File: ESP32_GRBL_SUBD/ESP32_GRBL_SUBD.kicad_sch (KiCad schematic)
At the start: 65 parts, among them J1 DB25_Female_MountingHoles, J10 Screw_Terminal_01x02, J11 Screw_Terminal_01x02, J12 Screw_Terminal_01x02, J13 Screw_Terminal_01x02, J14 Screw_Terminal_01x02, J2 Micro_SD_Card, J3 Conn_01x19_Female, J3a1 Conn_01x19_Female, J4 Conn_01x19_Female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

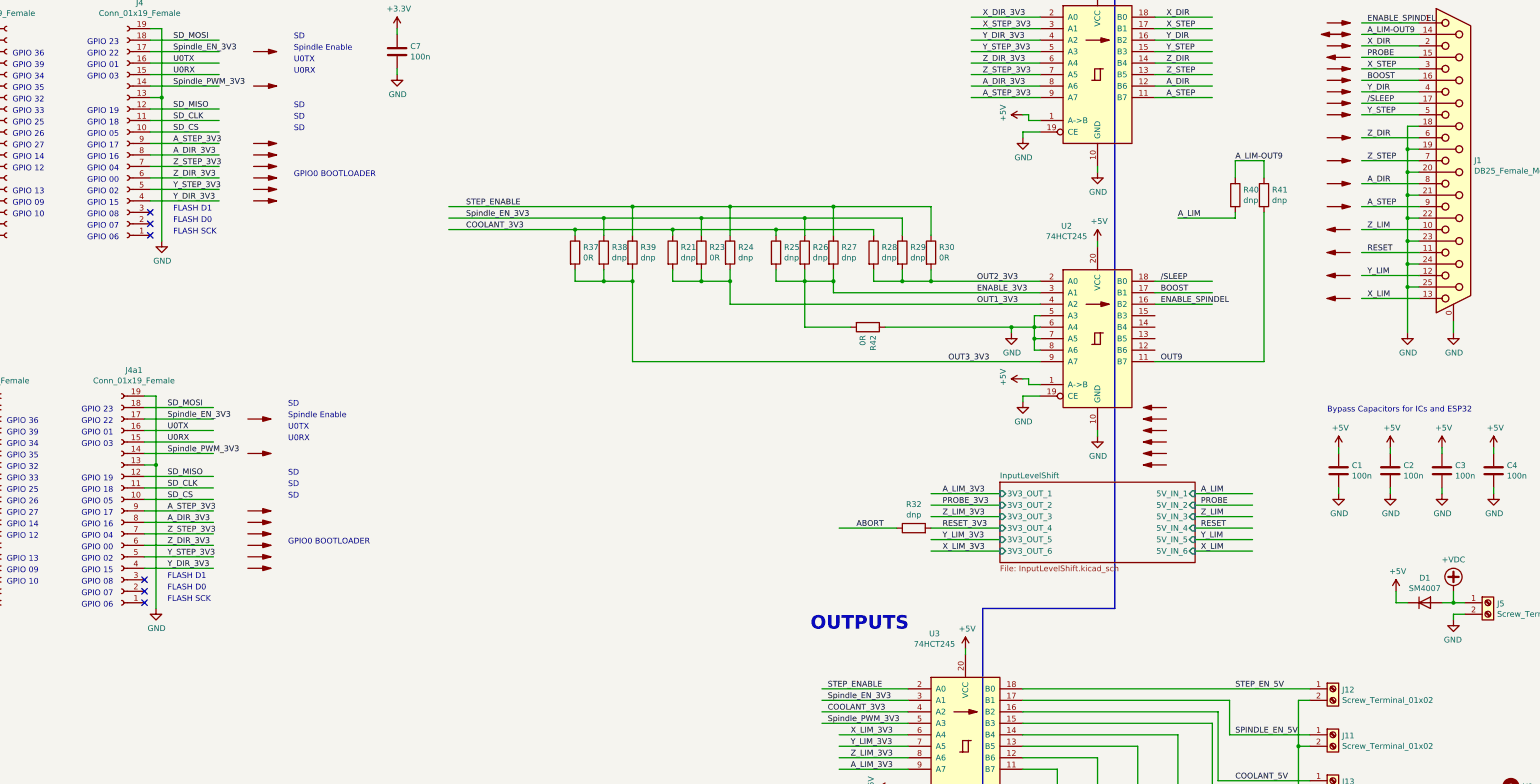
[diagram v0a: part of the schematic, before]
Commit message: wired Axis a to screw terminals
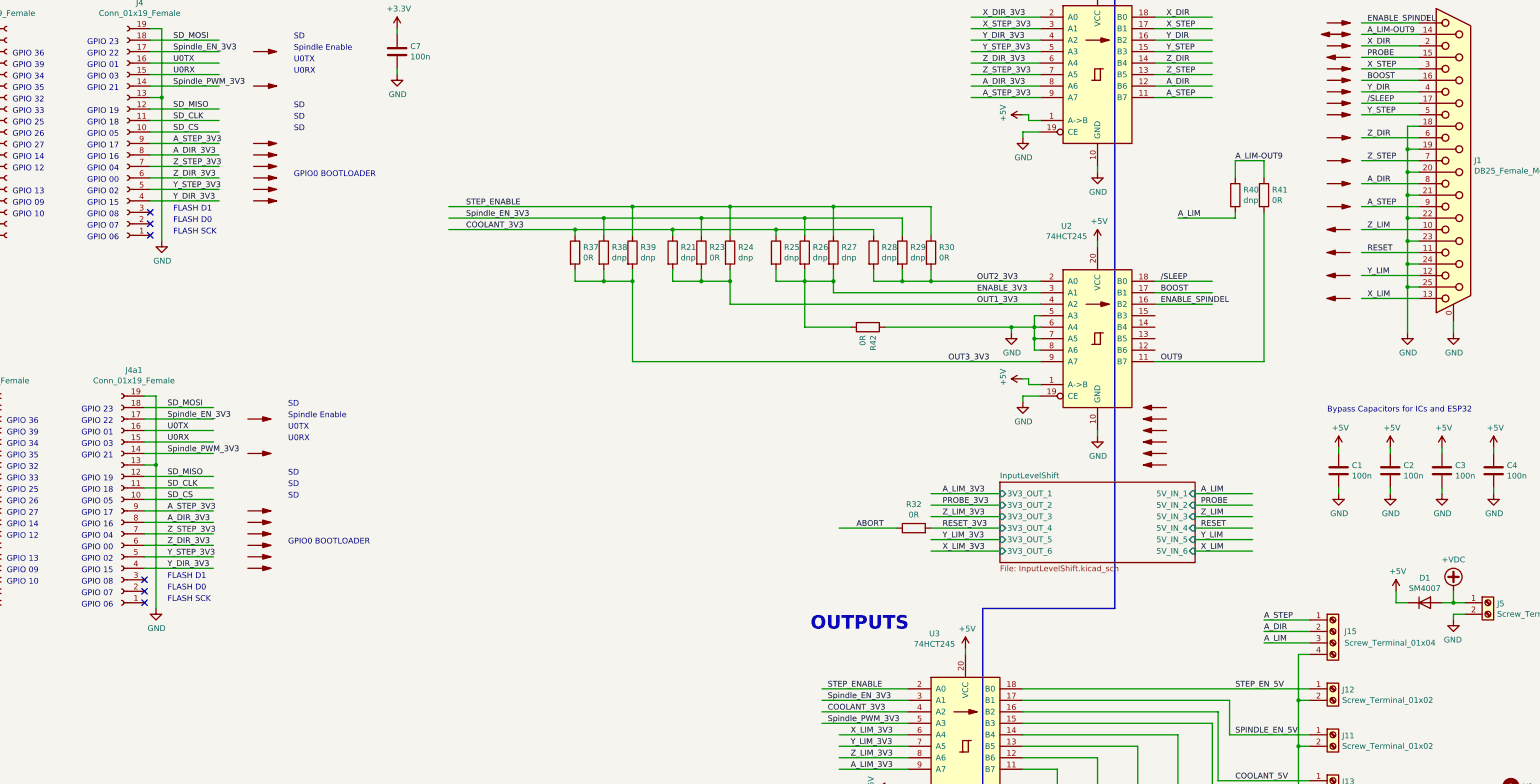
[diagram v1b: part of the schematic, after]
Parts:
- added J15: Screw_Terminal_01x04, TerminalBlock_MetzConnect:TerminalBlock_MetzConnect_Type055_RT01504HDWU_1x04_P5.00mm_Horizontal, symbol Connector:Screw_Terminal_01x04
- R32, R41: value dnp -> 0R
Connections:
- net A_DIR: now also J15.2 (Pin_2)
- net A_LIM: now also J15.3 (Pin_3)
- net A_STEP: now also J15.1 (Pin_1)
- net GND: now also J15.4 (Pin_4)
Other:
- note added: "GPIO 21"
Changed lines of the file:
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@@
   (junction (at 274.32 99.06) (diameter 0) (color 0 0 0 0)
   )
+  (junction (at 337.82 181.61) (diameter 0) (color 0 0 0 0)
+  )
   (junction (at 256.54 88.9) (diameter 0) (color 0 0 0 0)
   )
@@
     (stroke (width 0) (type default) (color 0 0 0 0))
   )
+  (wire (pts (xy 330.2 163.83) (xy 340.36 163.83))
+    (stroke (width 0) (type default) (color 0 0 0 0))
+  )
   (wire (pts (xy 149.86 72.39) (xy 190.5 72.39))
     (stroke (width 0) (type default) (color 0 0 0 0))
@@
     (stroke (width 0) (type default) (color 0 0 0 0))
   )
+  (wire (pts (xy 340.36 171.45) (xy 337.82 171.45))
+    (stroke (width 0) (type default) (color 0 0 0 0))
+  )
   (wire (pts (xy 67.31 247.65) (xy 90.17 247.65))
     (stroke (width 0) (type default) (color 0 0 0 0))
@@
     (stroke (width 0) (type default) (color 0 0 0 0))
   )
+  (wire (pts (xy 330.2 168.91) (xy 340.36 168.91))
+    (stroke (width 0) (type default) (color 0 0 0 0))
+  )
   (wire (pts (xy 31.75 60.96) (xy 46.99 60.96))
     (stroke (width 0) (type default) (color 0 0 0 0))
@@
     (stroke (width 0) (type default) (color 0 0 0 0))
   )
+  (wire (pts (xy 330.2 166.37) (xy 340.36 166.37))
+    (stroke (width 0) (type default) (color 0 0 0 0))
+  )
   (wire (pts (xy 276.86 189.23) (xy 311.15 189.23))
     (stroke (width 0) (type default) (color 0 0 0 0))
@@
     (stroke (width 0) (type default) (color 0 0 0 0))
   )
+  (wire (pts (xy 337.82 171.45) (xy 337.82 181.61))
+    (stroke (width 0) (type default) (color 0 0 0 0))
+  )
   (wire (pts (xy 264.16 212.09) (xy 264.16 214.63))
     (stroke (width 0) (type default) (color 0 0 0 0))
@@
     (effects (font (size 1.27 1.27)) (justify left bottom))
   )
+  (text "GPIO 21" (at 68.58 128.27 0)
+    (effects (font (size 1.27 1.27)) (justify left bottom))
+  )
   (text "SD" (at 114.3 116.84 0)
     (effects (font (size 1.27 1.27)) (justify left bottom))
@@
     (effects (font (size 1.27 1.27)) (justify left bottom))
   )
+  (text "GPIO 21" (at 69.85 46.99 0)
+    (effects (font (size 1.27 1.27)) (justify left bottom))
+  )
   (text "GPIO 09" (at 52.07 153.67 0)
     (effects (font (size 1.27 1.27)) (justify left bottom))
@@
     (effects (font (size 1.27 1.27)) (justify left bottom))
   )
+  (label "A_DIR" (at 330.2 166.37 0)
+    (effects (font (size 1.27 1.27)) (justify left bottom))
+  )
   (label "A_STEP_3V3" (at 88.9 58.42 0)
     (effects (font (size 1.27 1.27)) (justify left bottom))
@@
     (effects (font (size 1.27 1.27)) (justify left bottom))
   )
+  (label "A_LIM" (at 330.2 168.91 0)
+    (effects (font (size 1.27 1.27)) (justify left bottom))
+  )
   (label "BOOST" (at 353.06 44.45 0)
     (effects (font (size 1.27 1.27)) (justify left bottom))
@@
     (effects (font (size 1.27 1.27)) (justify left bottom))
   )
+  (label "A_STEP" (at 330.2 163.83 0)
+    (effects (font (size 1.27 1.27)) (justify left bottom))
+  )
   (label "Z_STEP_3V3" (at 88.9 63.5 0)
     (effects (font (size 1.27 1.27)) (justify left bottom))
@@
     (in_bom yes) (on_board yes)
     (property "Reference" "R32" (id 0) (at 252.73 138.2522 90))
-    (property "Value" "dnp" (id 1) (at 252.73 140.5636 90))
+    (property "Value" "0R" (id 1) (at 252.73 140.5636 90))
     (property "Footprint" "Resistor_SMD:R_0603_1608Metric" (id 2) (at 252.73 145.288 90)
       (effects (font (size 1.27 1.27)) hide)
@@
       (effects (font (size 1.27 1.27)) (justify left))
     )
-    (property "Value" "dnp" (id 1) (at 331.978 70.993 0)
+    (property "Value" "0R" (id 1) (at 331.978 70.993 0)
       (effects (font (size 1.27 1.27)) (justify left))
     )
@@
     )
   )
+  (symbol (lib_id "Connector:Screw_Terminal_01x04") (at 345.44 166.37 0) (unit 1)
+    (in_bom yes) (on_board yes) (fields_autoplaced)
+    (property "Reference" "J15" (id 0) (at 347.98 166.3699 0)
+      (effects (font (size 1.27 1.27)) (justify left))
+    )
+    (property "Value" "Screw_Terminal_01x04" (id 1) (at 347.98 168.9099 0)
+      (effects (font (size 1.27 1.27)) (justify left))
+    )
+    (property "Footprint" "TerminalBlock_MetzConnect:TerminalBlock_MetzConnect_Type055_RT01504HDWU_1x04_P5.00mm_Horizontal" (id 2) (at 345.44 166.37 0)
+      (effects (font (size 1.27 1.27)) hide)
+    )
+    (property "Datasheet" "~" (id 3) (at 345.44 166.37 0)
+      (effects (font (size 1.27 1.27)) hide)
+    )
+    (pin "1")
+    (pin "2")
+    (pin "3")
+    (pin "4")
+  )
   (symbol (lib_id "Connector:Screw_Terminal_01x02") (at 238.76 228.6 0) (unit 1)
     (in_bom yes) (on_board yes)
@@
       (reference "J14") (unit 1) (value "Screw_Terminal_01x02") (footprint "TerminalBlock_MetzConnect:TerminalBlock_MetzConnect_Type055_RT01502HDWU_1x02_P5.00mm_Horizontal")
     )
+    (path "/cfbb8e34-21a6-469a-90d0-36c5e2e8a754"
+      (reference "J15") (unit 1) (value "Screw_Terminal_01x04") (footprint "TerminalBlock_MetzConnect:TerminalBlock_MetzConnect_Type055_RT01504HDWU_1x04_P5.00mm_Horizontal")
+    )
     (path "/00000000-0000-0000-0000-00005f4ee6a6/00000000-0000-0000-0000-00005f4f5669"
       (reference "Q2") (unit 1) (value "BSS138") (footprint "Package_TO_SOT_SMD:SOT-23")
@@
     )
     (path "/00000000-0000-0000-0000-00005f0dcacb"
-      (reference "R32") (unit 1) (value "dnp") (footprint "Resistor_SMD:R_0603_1608Metric")
+      (reference "R32") (unit 1) (value "0R") (footprint "Resistor_SMD:R_0603_1608Metric")
     )
     (path "/00000000-0000-0000-0000-00005f3c9cfa"
@@
     )
     (path "/372ca174-dd9f-4c57-bc55-279c6f8b4e3a"
-      (reference "R41") (unit 1) (value "dnp") (footprint "Resistor_SMD:R_0603_1608Metric")
+      (reference "R41") (unit 1) (value "0R") (footprint "Resistor_SMD:R_0603_1608Metric")
     )
     (path "/6f7d2e2d-ab5c-405a-a7ee-a3211d67f7b6"
